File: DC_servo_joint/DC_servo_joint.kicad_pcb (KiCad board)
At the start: 2 copper layers, 61.5 x 53 mm, 49 parts, among them U1 AS5600, U2 ESP32-C3-WROOM-02, U3 SP3485EN, U5 TPS563200

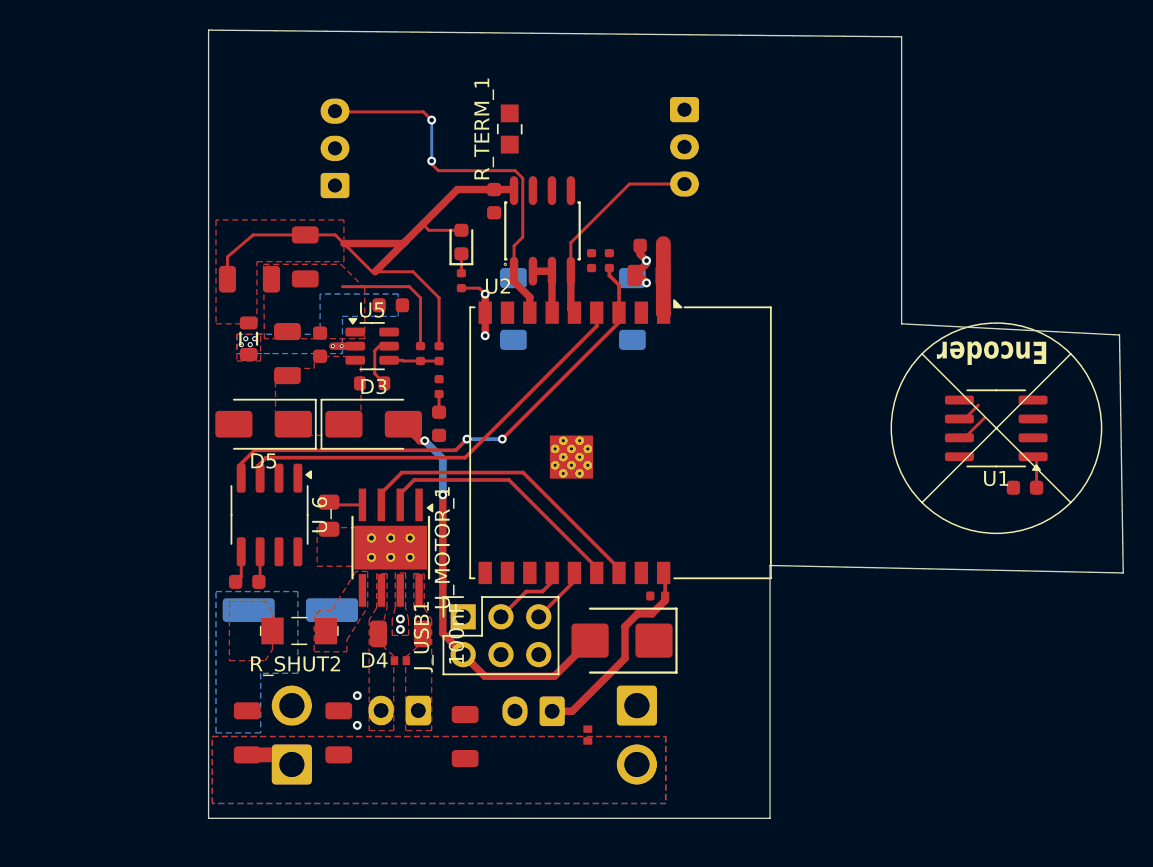
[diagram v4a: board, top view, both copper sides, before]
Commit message: Finalized Board outline. Fixed I2C signls. Roughtly figured out all compoent's location Still missing 3.3V stuff to be fixed
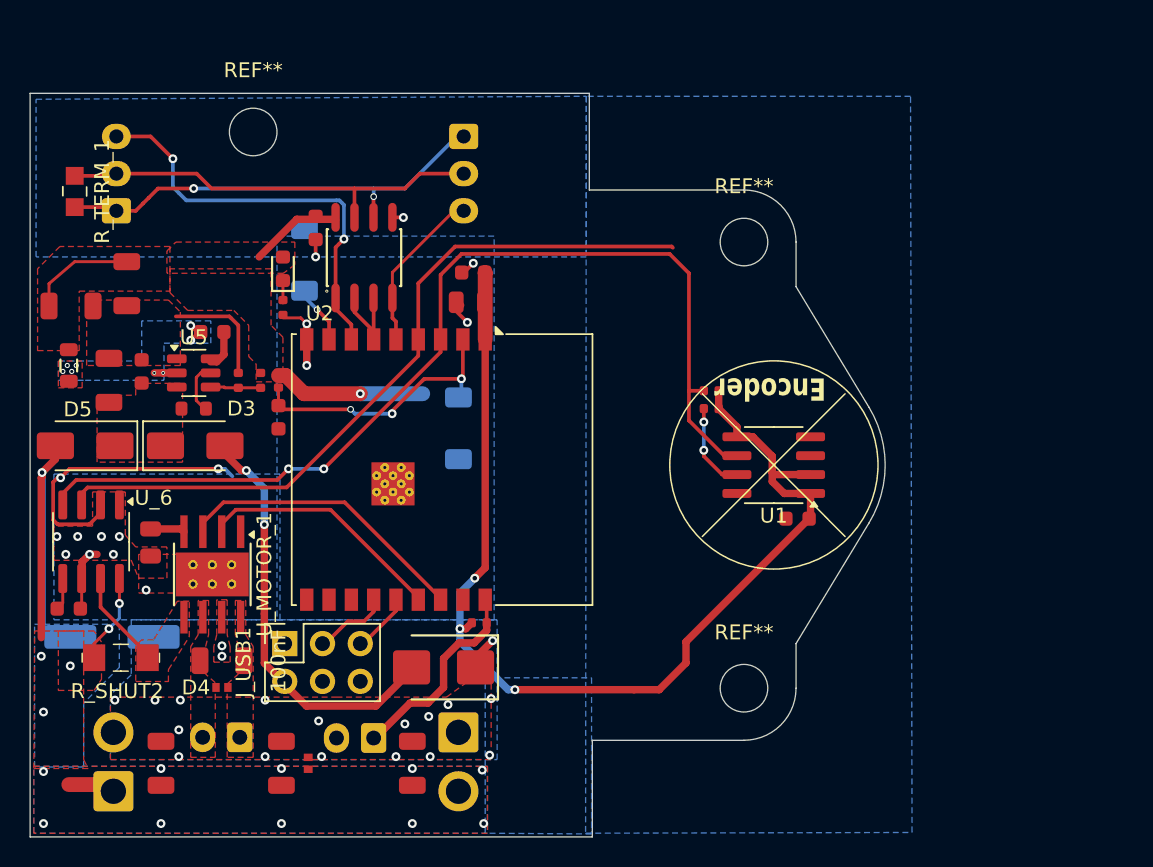
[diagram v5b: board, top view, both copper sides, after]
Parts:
- added REF**: MountingHole_3.2mm_M3, MountingHole:MountingHole_3.2mm_M3, F.Cu at (115.0, 52.6)
- added REF**: MountingHole_3.2mm_M3_DIN965, MountingHole:MountingHole_3.2mm_M3_DIN965, F.Cu at (148.0, 60.0)
- added REF**: MountingHole_3.2mm_M3_DIN965, MountingHole:MountingHole_3.2mm_M3_DIN965, F.Cu at (148.0, 90.0)
- moved R_TERM_1 29.5 mm to (103.0, 56.6), turned to -90 degrees
- moved D2 18.9 mm to (118.7, 95.0)
- moved C7 15.4 mm to (151.6, 78.6)
- moved U1 15.2 mm to (150.0, 75.0)
- moved J_BUS1 15.0 mm to (129.2, 52.9)
- moved J_BUS2 14.8 mm to (105.8, 57.9)
- moved S2 14.4 mm to (118.5, 61.2)
- moved S1 14.2 mm to (128.8, 72.5), turned to -90 degrees
- moved R_i2c2 12.8 mm to (145.8, 71.2), turned to 180 degrees
- moved C17 12.5 mm to (116.9, 95.0)
- moved R7 12.4 mm to (114.0, 69.3)
- moved L2 12.2 mm to (102.6, 68.3)
- moved D1 12.1 mm to (127.8, 88.6)
- moved C5 12.1 mm to (112.9, 88.2)
- moved C6 12.1 mm to (102.6, 84.7)
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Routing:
- net +3.3V: track 48.9 -> 98.3 mm, vias 0 -> 4
- net /SCL: track 35.9 -> 68.6 mm
- net +12V: track 3.27 -> 34.8 mm, vias 0 -> 16
- net /RS485A: track 0.00 -> 31.0 mm, vias 0 -> 2
- net /RS485B: track 0.00 -> 29.0 mm
- net /SDA: track 30.6 -> 56.6 mm, vias 0 -> 2
- net GND: track 19.3 -> 43.3 mm, vias 8 -> 35
- net /RST_BTM: track 1.22 -> 18.8 mm, vias 0 -> 3
- net /V_motor: track 0.00 -> 6.64 mm
- net /BOOT_BTM: track 0.00 -> 3.96 mm, vias 0 -> 1
- net /UART_TX: track 14.1 -> 11.4 mm
- net Net-(U5-VBST): track 0.00 -> 2.41 mm
- net /UART_RX: track 25.7 -> 28.0 mm
- net /485_RE_DE: track 4.09 -> 6.13 mm
- net /TPS_SW: track 1.51 -> 3.26 mm, vias 6 -> 8
- added copper zone on B.Cu, net GND
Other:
- board size 61.5 x 53 mm -> 57.5 x 50 mm

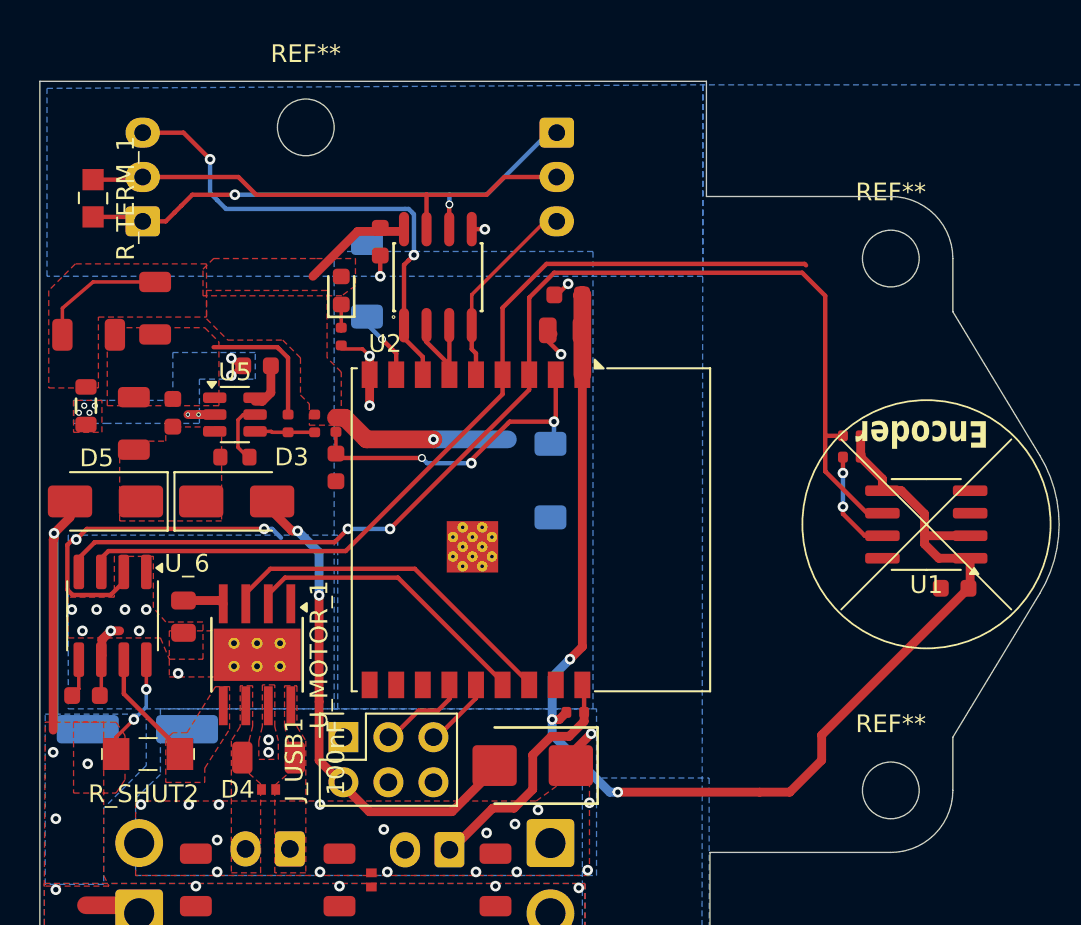
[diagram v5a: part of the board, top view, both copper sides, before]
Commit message: Fixed missing tarce, added in some skilscreen fix
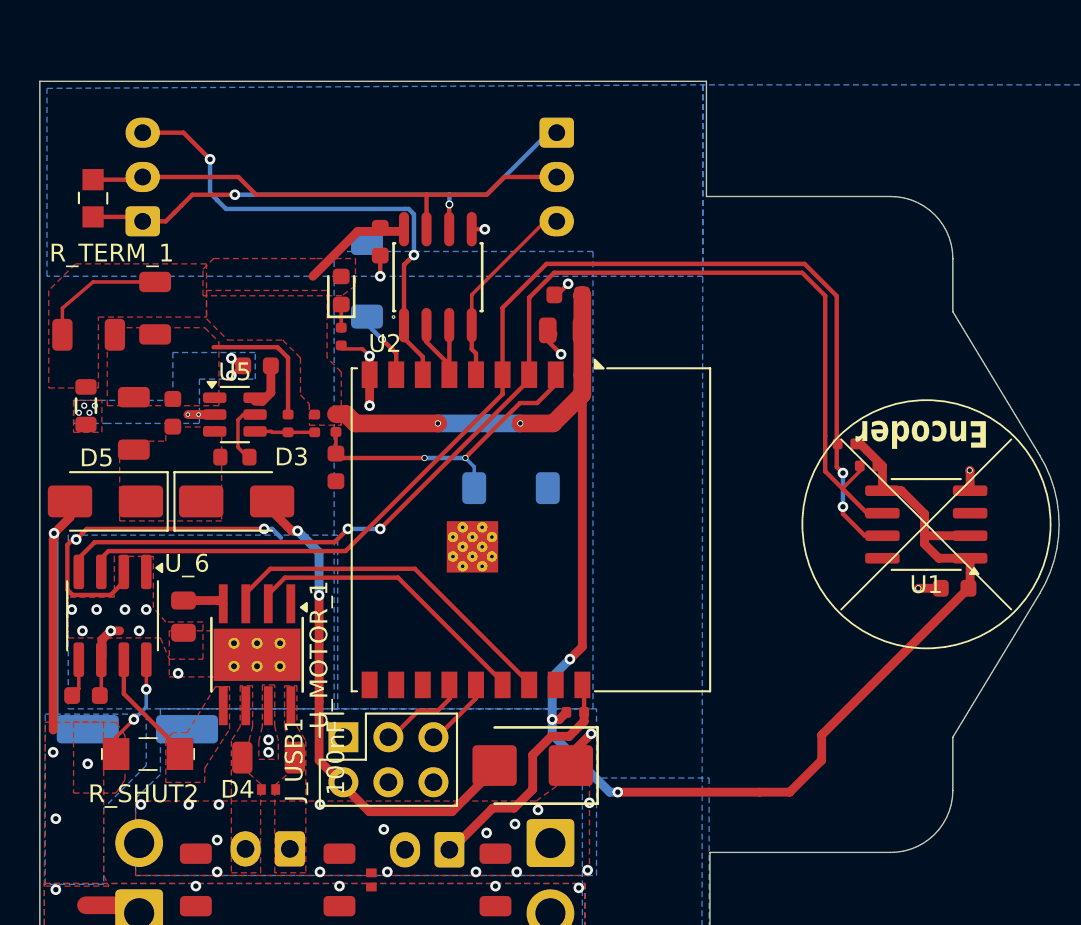
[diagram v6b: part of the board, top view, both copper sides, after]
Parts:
- removed REF**: MountingHole_3.2mm_M3, MountingHole:MountingHole_3.2mm_M3
- removed REF** (x2): MountingHole_3.2mm_M3_DIN965, MountingHole:MountingHole_3.2mm_M3_DIN965
- moved S1 2.27 mm to (126.6, 73.0), turned to 0 degrees
- moved R_i2c1 1.95 mm to (146.8, 71.7)
- moved R_i2c2 0.81 mm to (145.5, 70.5)
- renumbered TH1 to J_NTC1
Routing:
- net /SDA: track 56.6 -> 68.3 mm
- net +3.3V: track 98.3 -> 103.9 mm, vias 4 -> 5
- net GND: track 43.3 -> 45.7 mm, vias 35 -> 37
- net /RST_BTM: track 18.8 -> 18.0 mm, vias 3 -> 2
- net /SCL: track 68.6 -> 69.1 mm
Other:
- board text added: "BOOT"
- board text added: "RST"

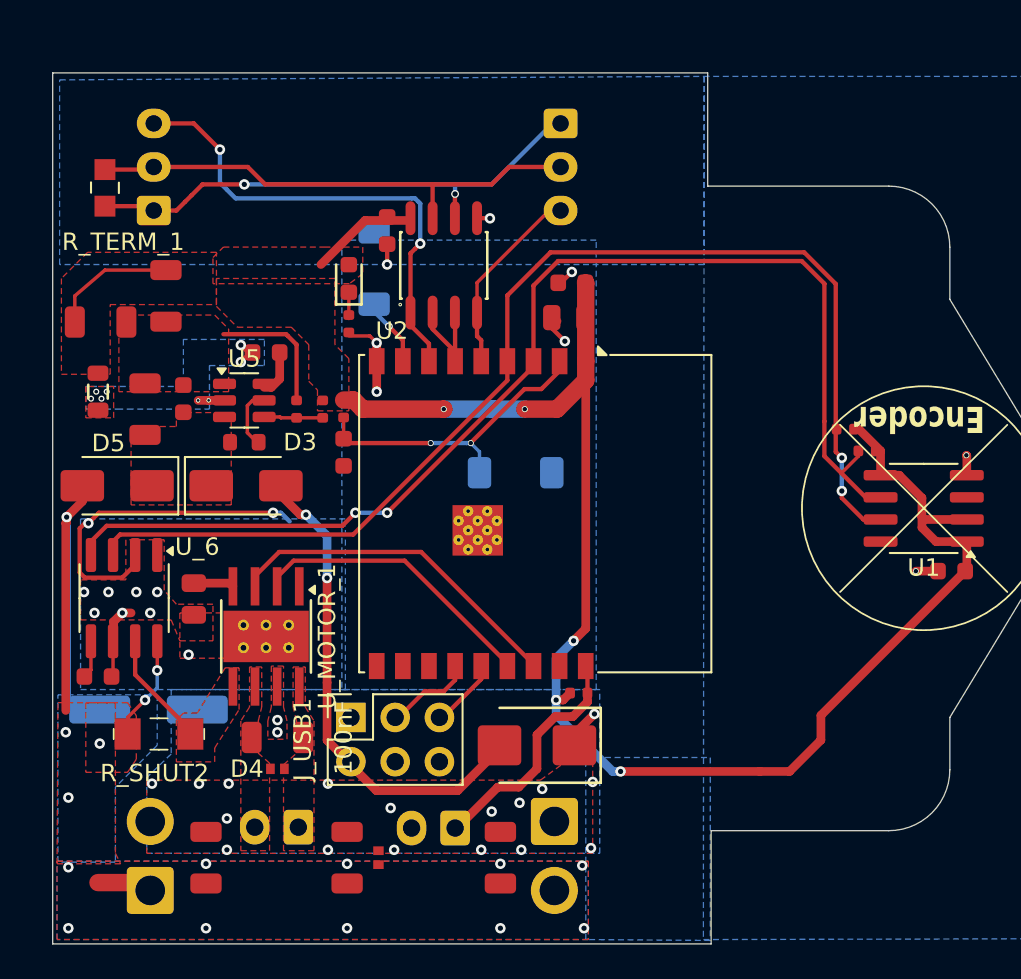
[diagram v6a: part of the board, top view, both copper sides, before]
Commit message: Fix the 3.3V power layout
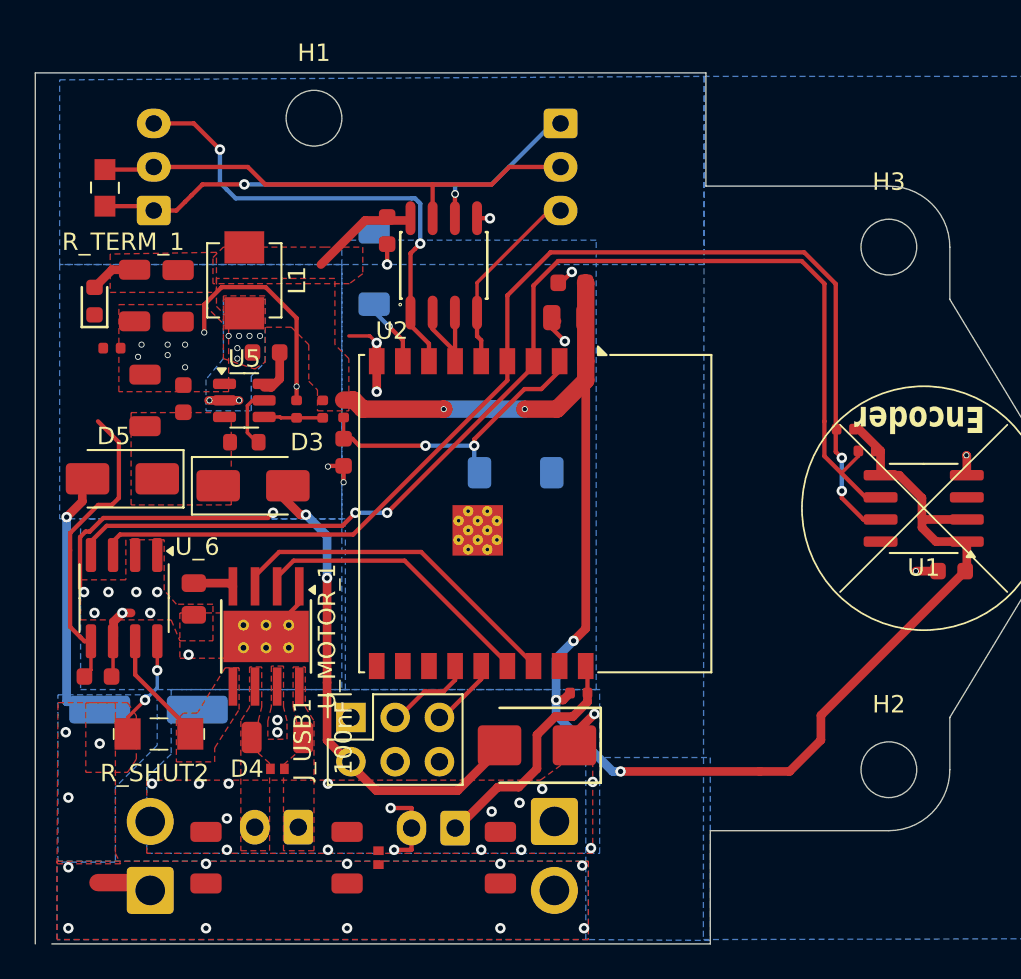
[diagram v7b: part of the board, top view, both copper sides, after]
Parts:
- removed L2: 2.2uH,50mA, PCM_JLCPCB:L_0805
- added H1: M3 Mount, MountingHole:MountingHole_3.2mm_M3_DIN965, F.Cu at (115.0, 52.6)
- added H2: M3 Mount, MountingHole:MountingHole_3.2mm_M3_DIN965, F.Cu at (148.0, 90.0)
- added H3: M3 Mount, MountingHole:MountingHole_3.2mm_M3_DIN965, F.Cu at (148.0, 60.0)
- added L1: 2.2uH, Inductor_SMD:L_Vishay_IHLP-1616, F.Cu at (111.0, 61.9)
- moved D6 14.7 mm to (102.4, 63.1)
- moved R6 13.7 mm to (103.4, 65.8), turned to 0 degrees
- moved C3 2.47 mm to (104.7, 62.8), turned to -90 degrees
- moved C10 0.70 mm to (107.2, 62.8)
- moved D5 0.50 mm to (104.0, 73.3)
- moved C9 0.50 mm to (105.3, 68.8)
- moved D3 0.40 mm to (111.5, 73.7)
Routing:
- net GND: track 45.7 -> 57.1 mm, vias 37 -> 46
- net +12V: track 34.8 -> 23.7 mm
- net +3.3V: track 103.9 -> 114.8 mm
- net Net-(D6-Pad1): track 1.31 -> 0.00 mm
- net /TPS_SW: track 3.26 -> 2.12 mm
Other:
- board size 57.5 x 50 mm -> 58.5 x 50 mm

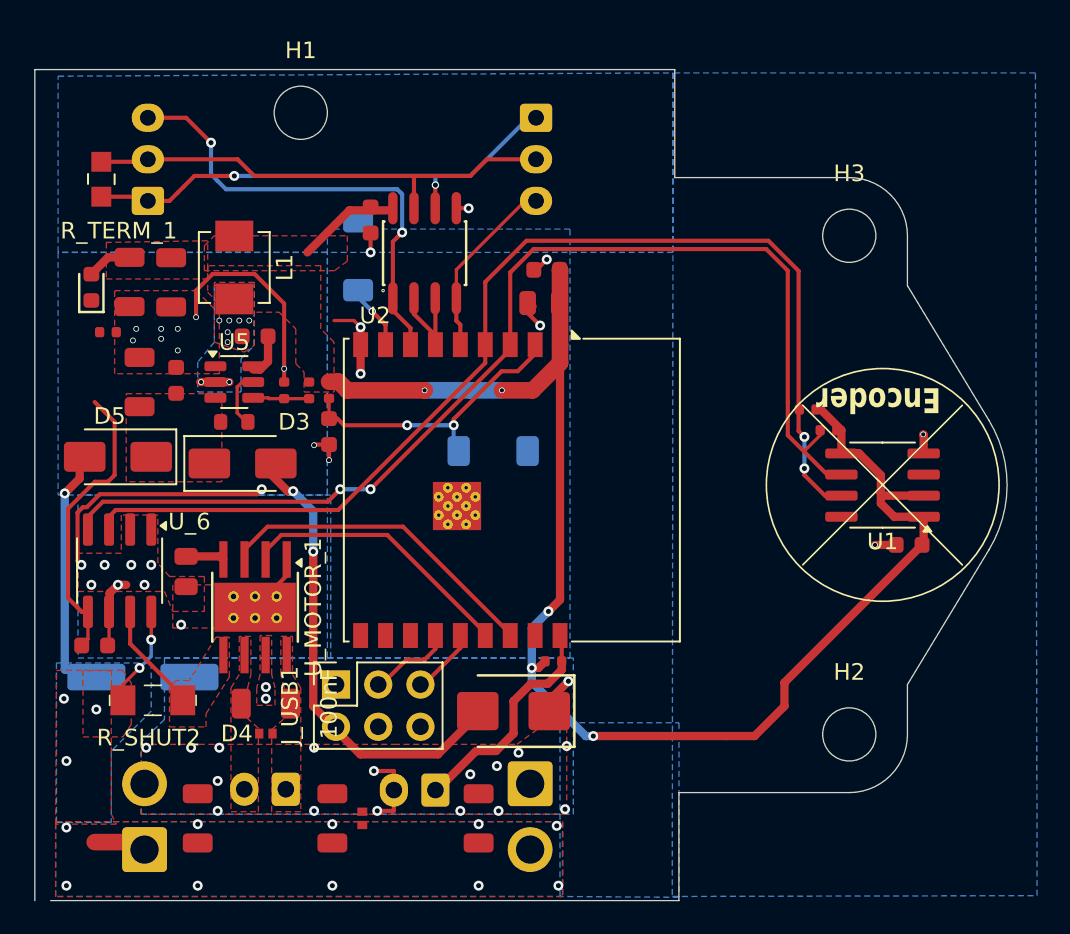
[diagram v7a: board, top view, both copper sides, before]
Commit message: Update Big cap selection. Better layout of power trace. Update silk screen. Fix lots of DRC vialation.
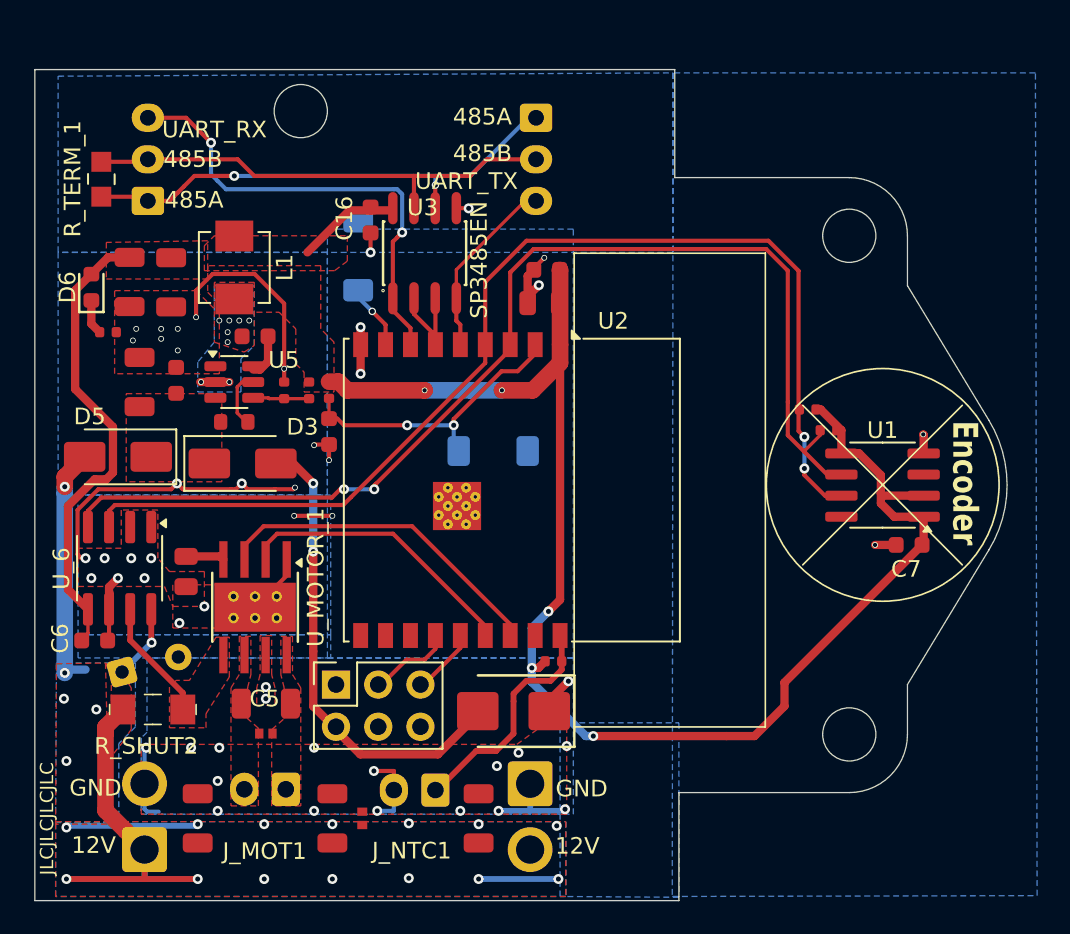
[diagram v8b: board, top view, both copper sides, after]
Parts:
- removed C11: 47uf, Capacitor_SMD:CP_Elec_6.3x5.4
- added C15: 47uF, Capacitor_THT:CP_Radial_D8.0mm_P3.50mm, B.Cu at (104.2, 86.2)
- moved R_SHUT2 0.55 mm to (106.1, 88.5)
- moved C6 0.30 mm to (102.6, 84.3)
- moved U_6 0.15 mm to (104.1, 80.0)
- moved H1 0.10 mm to (115.0, 52.5)
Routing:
- net +12V: track 23.7 -> 61.3 mm, vias 16 -> 20
- net GND: track 57.1 -> 70.3 mm, vias 46 -> 50
- net +3.3V: track 114.8 -> 122.6 mm
- net Net-(D6-Pad1): track 0.00 -> 2.12 mm
- net /RS485A: track 31.0 -> 29.5 mm
- net /RST_BTM: track 18.4 -> 17.0 mm
- net /usb_5v: track 27.5 -> 28.8 mm
- net /485_RE_DE: track 6.13 -> 5.35 mm
- net /UART_RX: track 28.0 -> 27.3 mm
- net /UART_TX: track 11.4 -> 10.7 mm
- net /V_motor: track 6.64 -> 7.34 mm
- net Net-(U5-VFB): track 3.95 -> 3.38 mm
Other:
- outline, holes or cut-outs redrawn
- board text added: "12V"
- board text added: "485A"
- board text added: "485B"
- board text added: "GND"
- board text added: "JLCJLCJLCJLC"
- board text added: "J_MOT1"
- board text added: "J_NTC1"
- board text added: "UART_RX"
- board text added: "UART_TX"
